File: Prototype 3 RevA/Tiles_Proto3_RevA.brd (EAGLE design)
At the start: 40 x 40 mm, 40 parts, among them U2 MF-DSC-SOT233-MMBT3904

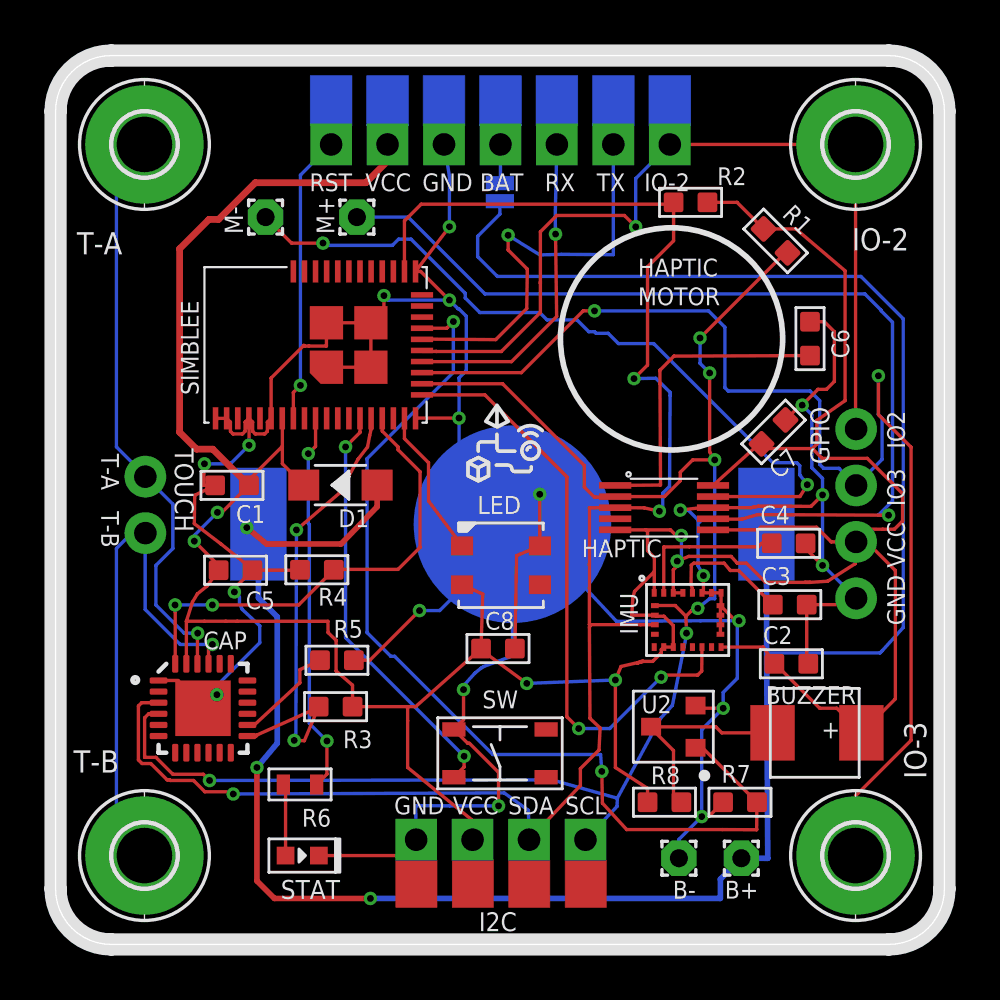
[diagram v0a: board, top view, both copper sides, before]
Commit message: added tiles dock
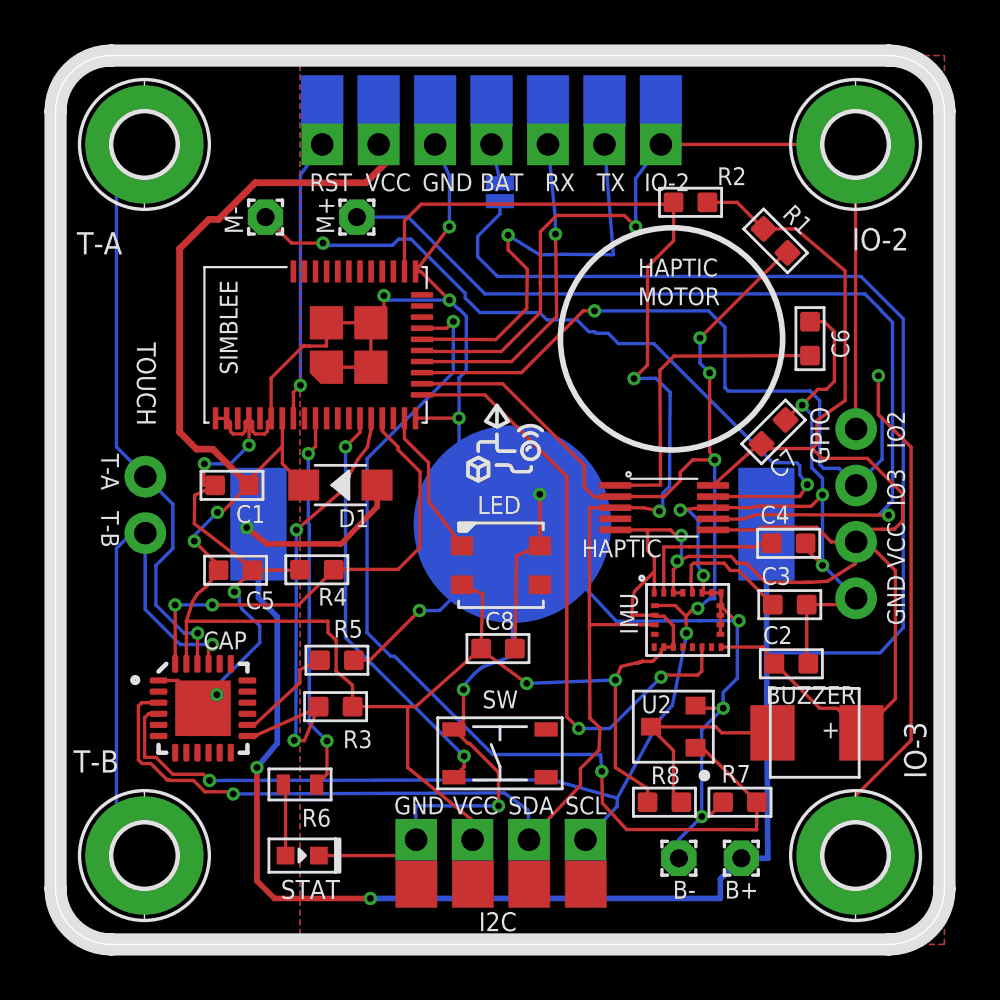
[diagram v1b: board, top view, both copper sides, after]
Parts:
- J1: device tiles:1X07_NO_SILK_SQUAREPADS -> tiles:1X07_SQUAREPADS_BOTTOM
- moved J1 0.40 mm to (12.0, -4.00)
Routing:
- added copper zone on layer 1, net GND
- added copper zone on layer 16, net GND

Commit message: increased holes to 3mm
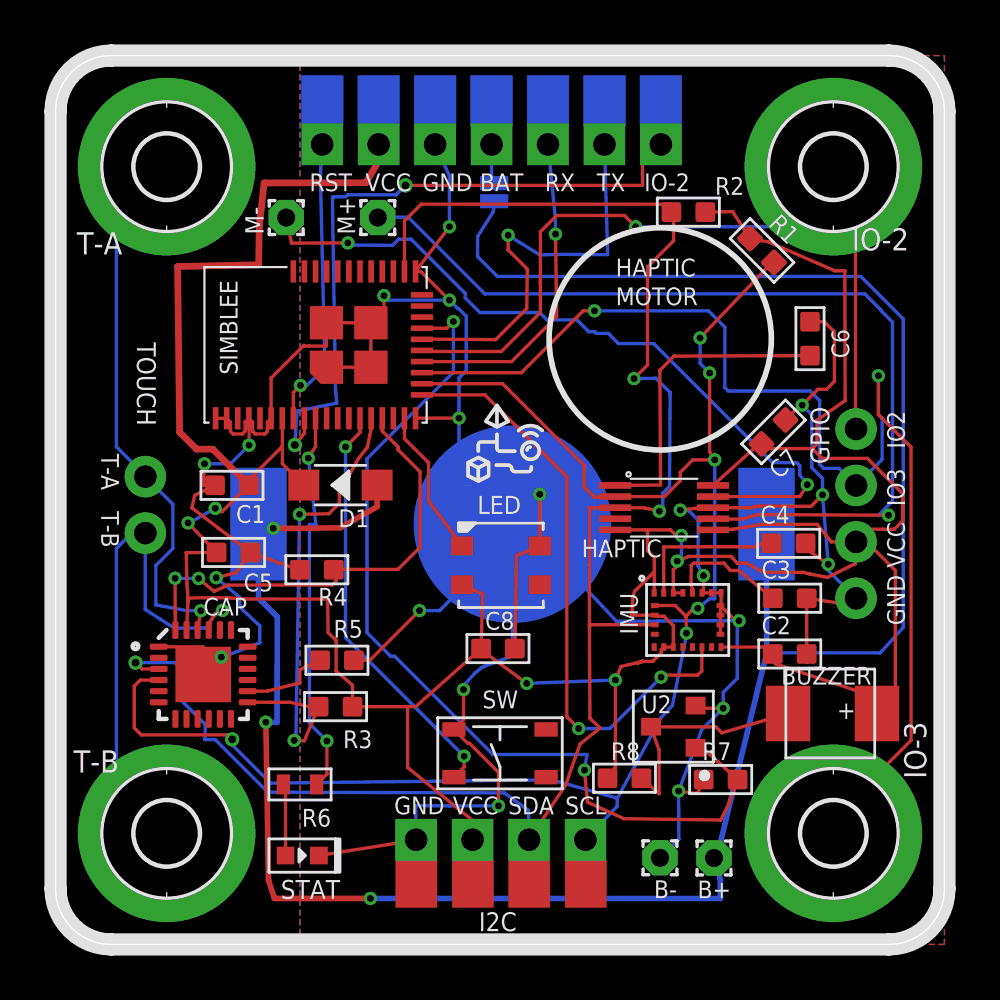
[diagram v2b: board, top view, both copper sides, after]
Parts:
- moved R8 2.10 mm to (25.6, -32.5)
- moved CAP 1.52 mm to (6.64, -27.9)
- moved CAP-A 1.41 mm to (5.00, -5.00)
- moved CAP-B 1.41 mm to (5.00, -35.0)
- moved IO-2 1.41 mm to (35.0, -5.00)
- moved IO-3 1.41 mm to (35.0, -35.0)
- moved R7 1.34 mm to (29.9, -32.6)
- moved B+ 1.23 mm to (29.6, -36.1)
- moved BUZZER 1.12 mm to (35.1, -29.8)
- moved M+ 0.94 mm to (14.5, -7.29)
- moved M- 0.93 mm to (10.4, -7.29)
- moved B- 0.85 mm to (27.2, -36.1)
- moved C5 0.81 mm to (8.01, -22.4)
- moved R1 0.75 mm to (31.8, -8.77)
- moved R2 0.45 mm to (28.5, -7.04)
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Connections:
- net FACTORY: now also J1.7
- net IO-2: no longer J1.7
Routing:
- net FACTORY: track 0.00 -> 30.3 mm, vias 0 -> 2
- net V_BATT: track 110.9 -> 107.7 mm
- net IO-2: track 40.8 -> 37.6 mm
- net BUZZER: track 44.6 -> 42.0 mm
- net GND: track 174.7 -> 176.8 mm
- net CAP-B: track 24.0 -> 25.2 mm
- net SCL: track 73.5 -> 74.7 mm
- net N$4: track 9.54 -> 10.5 mm
- net N$8: track 43.4 -> 42.5 mm
- net CAP-A: track 26.5 -> 27.4 mm
- net IO-3: track 55.9 -> 55.2 mm
- net N$3: track 4.70 -> 3.99 mm
- net VCC: track 165.4 -> 164.8 mm
